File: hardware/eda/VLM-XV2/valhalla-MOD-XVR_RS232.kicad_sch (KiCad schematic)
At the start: 23 parts, among them J1 RS-232, J2 POLOLU-4941, J3 TTL, J4 BUS, U1 74LS06, U2 L78L33_TO92, U3 *2

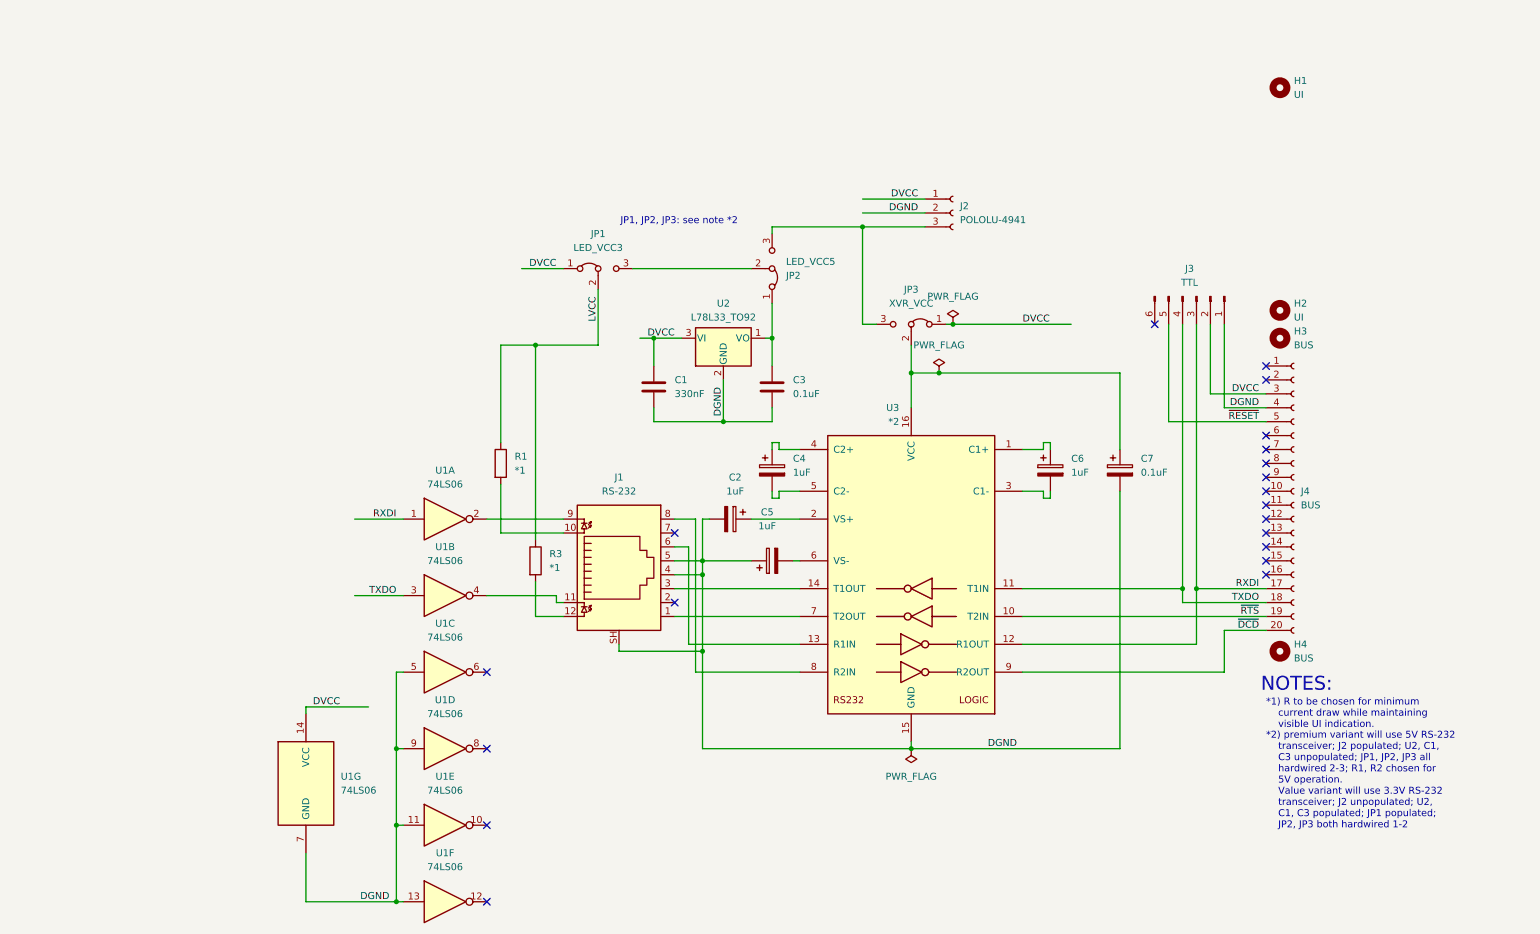
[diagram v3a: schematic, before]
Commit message: UPDATE: updated MOD-XVR(RS232) to match the latest specification.
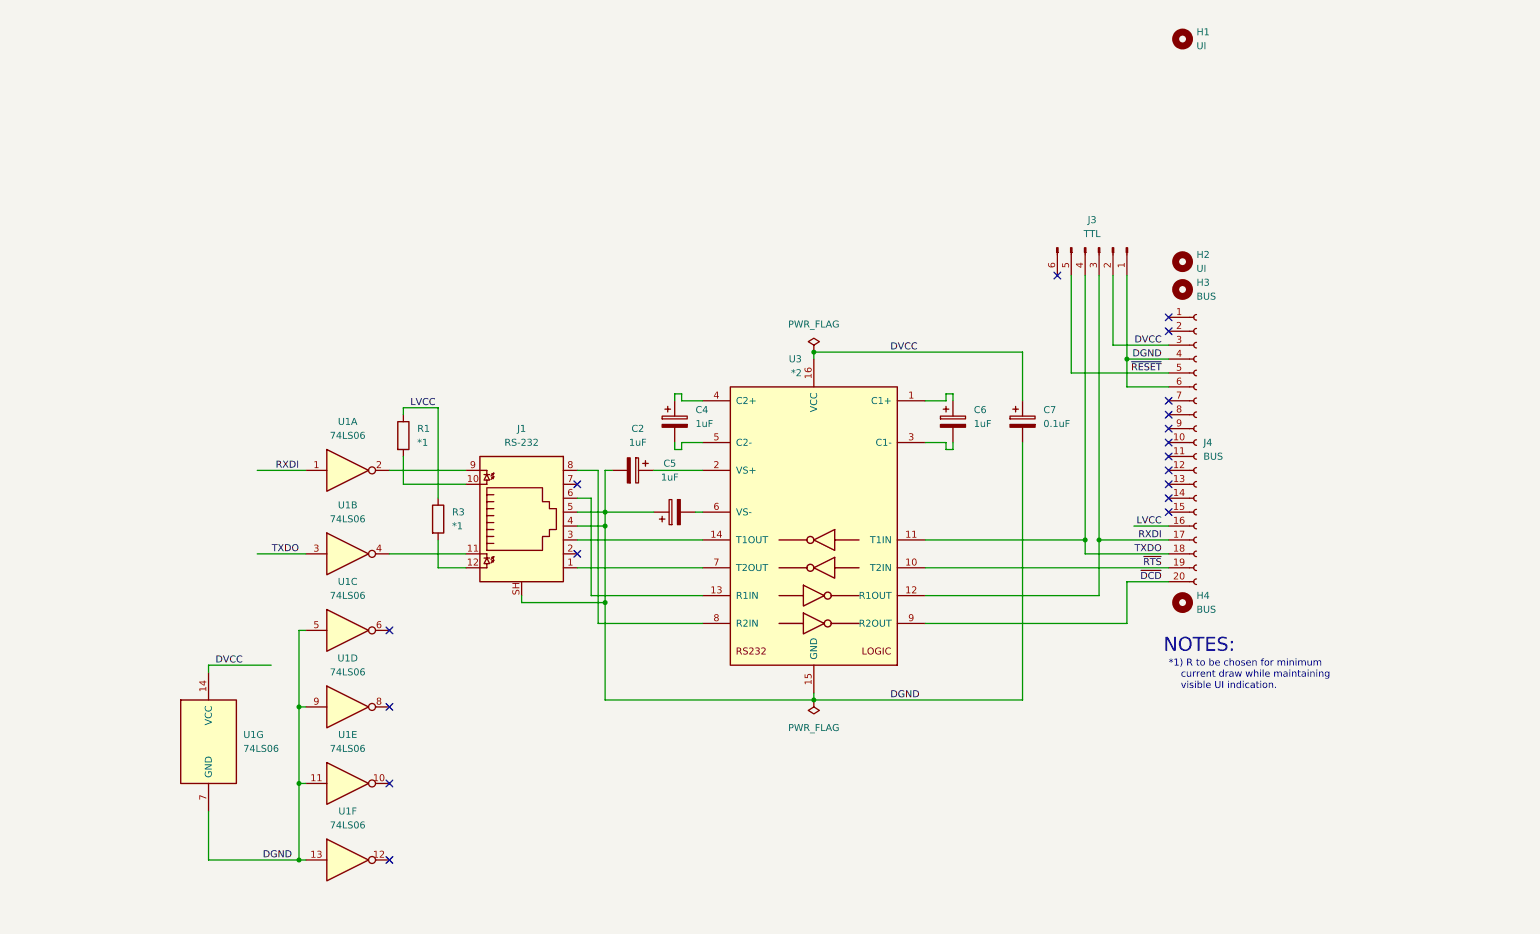
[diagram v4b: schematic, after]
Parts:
- removed C1: 330nF, Capacitor_THT:C_Rect_L4.6mm_W2.0mm_P2.50mm_MKS02_FKP02, symbol Device:C
- removed C3: 0.1uF, Capacitor_THT:C_Rect_L4.6mm_W2.0mm_P2.50mm_MKS02_FKP02, symbol Device:C
- removed J2: POLOLU-4941, Connector_PinSocket_2.54mm:PinSocket_1x03_P2.54mm_Horizontal, symbol Connector:Conn_01x03_Socket
- removed JP1: LED_VCC3, Connector_PinHeader_2.54mm:PinHeader_1x03_P2.54mm_Vertical, symbol Jumper:Jumper_3_Bridged12
- removed JP2: LED_VCC5, Jumper:SolderJumper-3_P1.3mm_Open_RoundedPad1.0x1.5mm, symbol Jumper:Jumper_3_Bridged12
- removed JP3: XVR_VCC, Jumper:SolderJumper-3_P1.3mm_Open_RoundedPad1.0x1.5mm, symbol Jumper:Jumper_3_Bridged12
- removed U2: L78L33_TO92, Package_TO_SOT_THT:TO-92_Wide, symbol Regulator_Linear:L78L33_TO92
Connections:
- net DGND: now also J4.6 (Pin_6)
- net DVCC: now also C7.1, U3.16 (VCC)
- net LVCC: now also J4.16 (Pin_16)
- no-connect marks 20 -> 18
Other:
- note removed: "*2) premium variant will use 5V RS-232 transceiver; J2 populated; U2, C1, C3 unpopulated; JP1, JP2, JP3 all hardwired 2-3; R1, R2 chosen for 5V operation. Value variant will use 3.3V RS-232 transceiver; J2 unpopulated; U2, C1, C3 populated; JP1 populated; JP2, JP3 both hardwired 1-2"
- note removed: "JP1, JP2, JP3: see note *2"
- title: (none) -> Valhalla MOD-XVR(RS232)
- moved on the sheet: C2, C4, C5, C6, C7, H1, H2, H3, H4, J1, J3, J4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
